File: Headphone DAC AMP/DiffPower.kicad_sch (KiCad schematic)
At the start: 11 parts, among them U6 MCP1727-1802xSN, U7 MCP1727-3302xSN, U9 TPS717XX

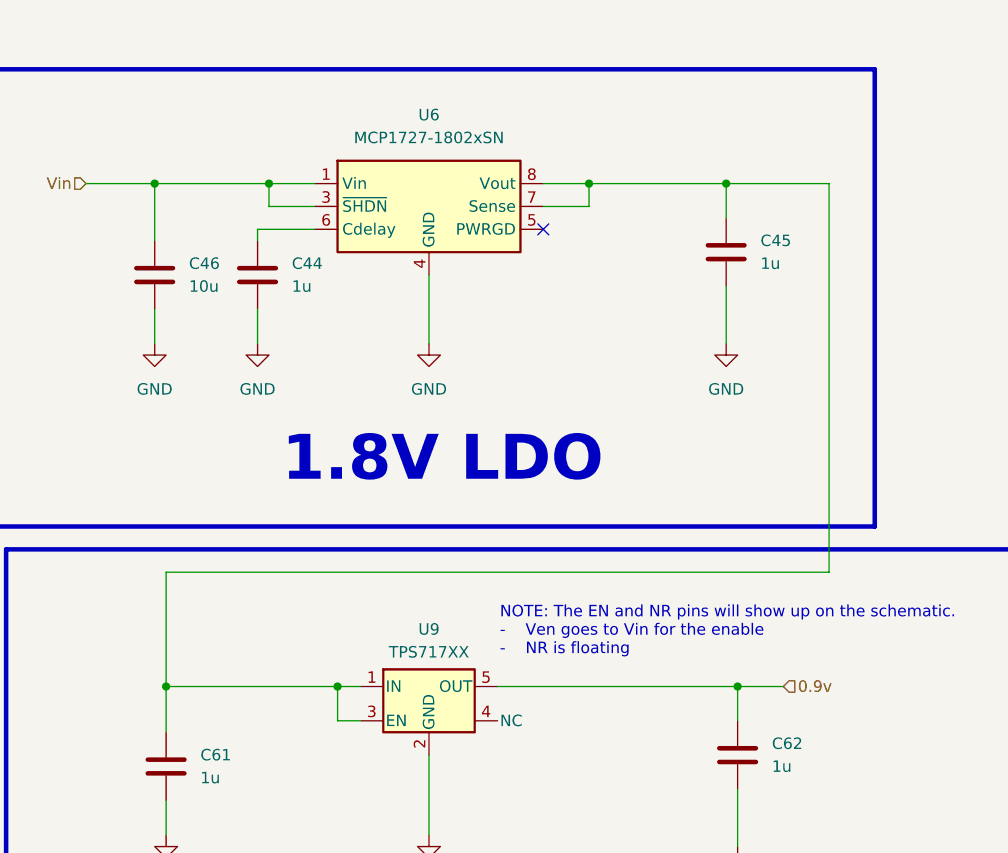
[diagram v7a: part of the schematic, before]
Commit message: Footprints & Placements
All footprints are loaded in PCB error free, some PCB mistakes were fixed, and worked on the placements for the TPA6120, the XMOS, the DAC, and the outputs
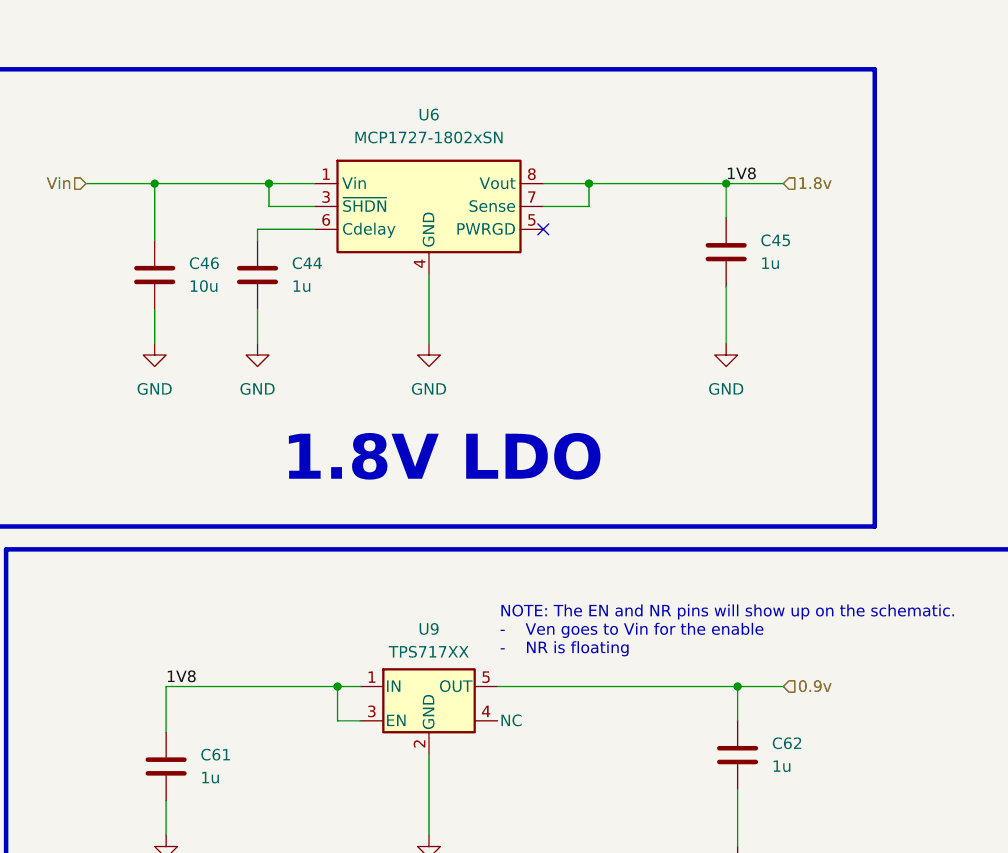
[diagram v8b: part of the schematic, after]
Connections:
- net 1.8v: now reaches C45.1, C61.1, U6.7 (Sense), U6.8 (Vout), U9.1 (IN), U9.3 (EN)
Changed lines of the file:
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@@
-	)
-	(junction
-		(at 40.64 148.59)
-		(diameter 0)
-		(color 0 0 0 0)
 	)
 	(junction
@@
 	(wire
 		(pts
-			(xy 40.64 135.89) (xy 114.3 135.89)
-		)
-		(stroke
-			(width 0)
-			(type default)
-		)
-	)
-	(wire
-		(pts
-			(xy 114.3 92.71) (xy 102.87 92.71)
+			(xy 109.22 92.71) (xy 102.87 92.71)
 		)
 		(stroke
@@
 	(wire
 		(pts
-			(xy 40.64 148.59) (xy 40.64 135.89)
-		)
-		(stroke
-			(width 0)
-			(type default)
-		)
-	)
-	(wire
-		(pts
 			(xy 31.75 92.71) (xy 39.37 92.71)
 		)
@@
 	(wire
 		(pts
-			(xy 114.3 135.89) (xy 114.3 92.71)
-		)
-		(stroke
-			(width 0)
-			(type default)
-		)
-	)
-	(wire
-		(pts
 			(xy 59.69 148.59) (xy 40.64 148.59)
 		)
@@
 			(width 0)
 			(type default)
+		)
+	)
+	(label "1V8"
+		(at 40.64 148.59 0)
+		(effects
+			(font
+				(size 1.27 1.27)
+			)
+			(justify left bottom)
+		)
+	)
+	(label "1V8"
+		(at 102.87 92.71 0)
+		(effects
+			(font
+				(size 1.27 1.27)
+			)
+			(justify left bottom)
 		)
 	)
@@
 		)
 	)
+	(hierarchical_label "1.8v"
+		(shape input)
+		(at 109.22 92.71 0)
+		(effects
+			(font
+				(size 1.27 1.27)
+			)
+			(justify left)
+		)
+	)
